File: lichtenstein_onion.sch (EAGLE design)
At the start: 58 parts, among them IC1 LM2852Y-3V3, IC2 MCP23017, J1 MAGJACK, U1 ONION-OMEGA2

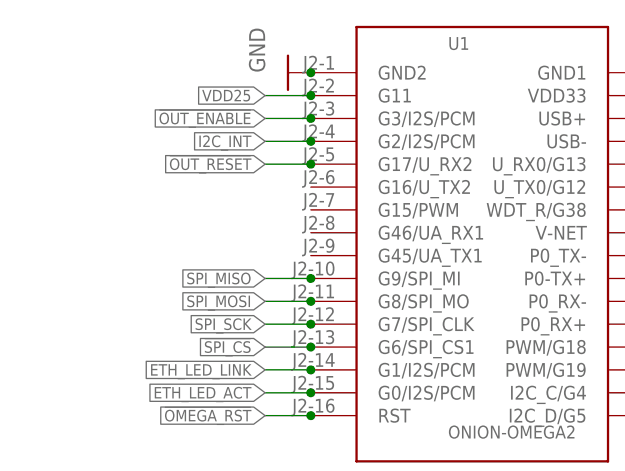
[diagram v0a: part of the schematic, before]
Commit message: Cleaned up traces slightly for PWM board
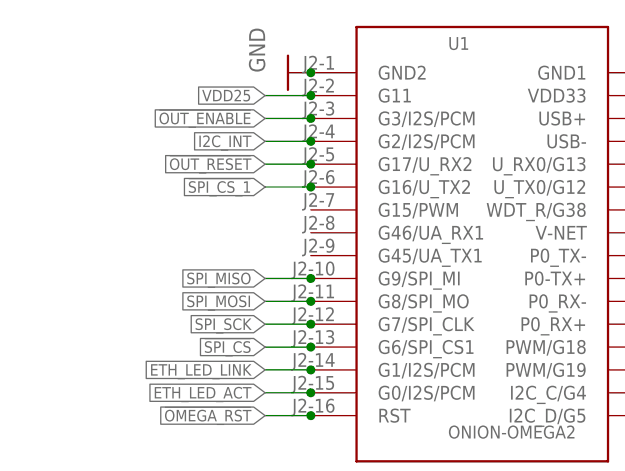
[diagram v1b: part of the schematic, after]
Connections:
- new net !SPI_CS_1: U1.G16/U_TX2
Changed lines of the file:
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@@
+</segment>
+</net>
+<net name="!SPI_CS_1" class="0">
+<segment>
+<pinref part="U1" gate="G$1" pin="G16/U_TX2"/>
+<wire x1="35.56" y1="160.02" x2="30.48" y2="160.02" width="0.1524" layer="91"/>
+<label x="30.48" y="160.02" size="1.27" layer="95" rot="R180" xref="yes"/>
+<junction x="35.56" y="160.02"/>
 </segment>
 </net>
